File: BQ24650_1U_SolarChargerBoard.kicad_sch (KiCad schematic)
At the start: 33 parts, among them J1 Solar IO, J2 Battery IO, Q1 Q_NMOS_GDS, Q2 Q_NMOS_GDS, Q3 Q_NMOS_GDS, U1 BQ24650

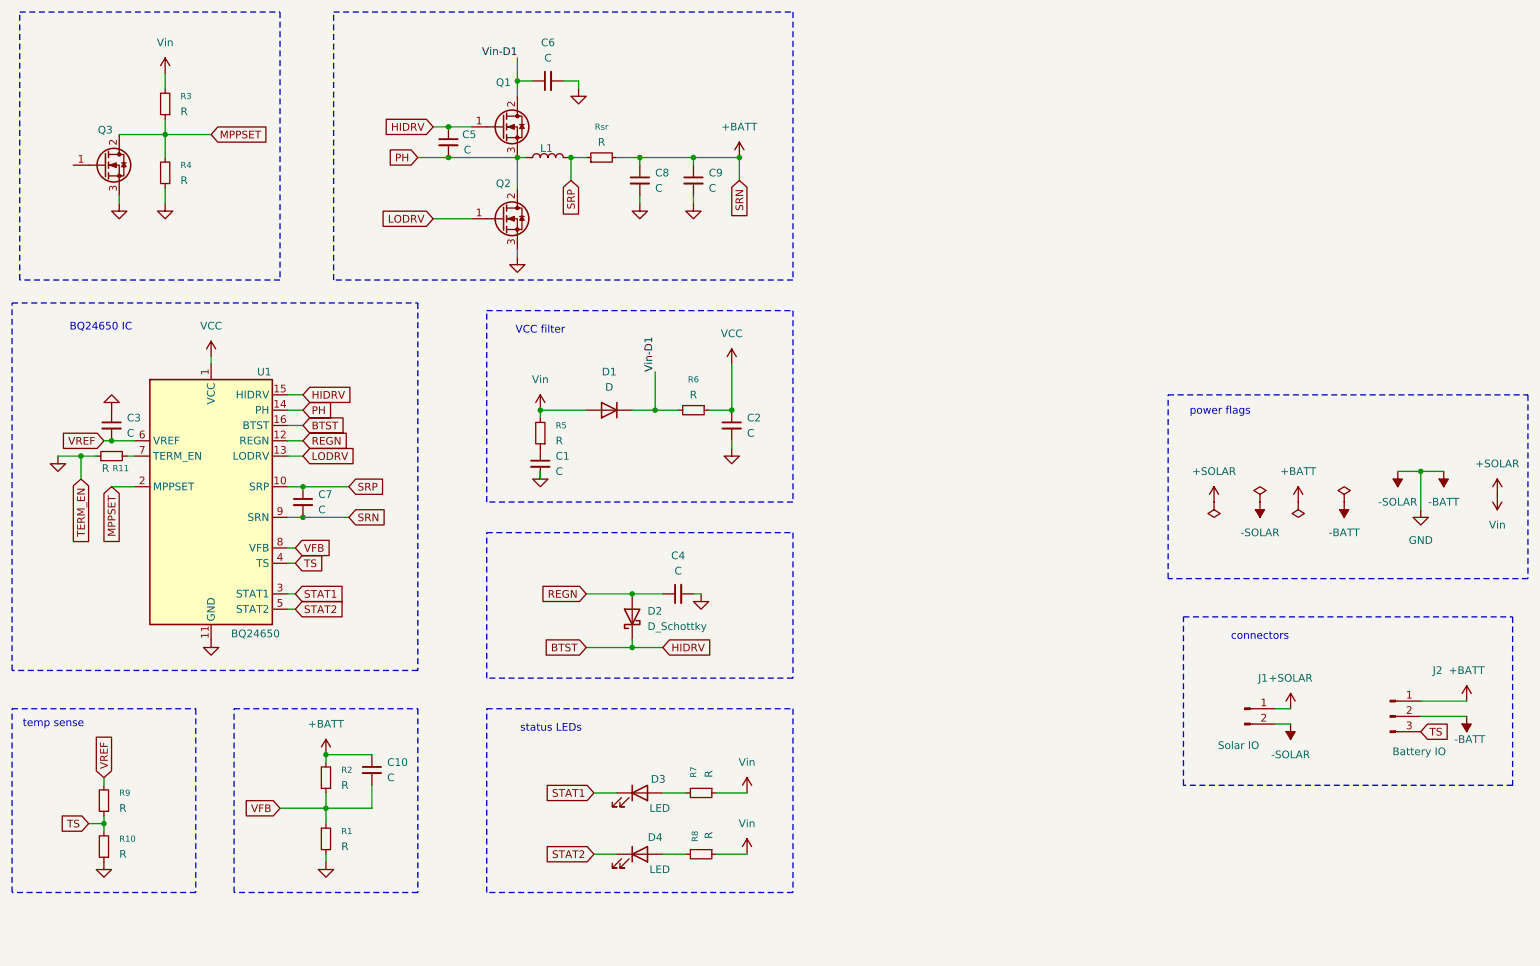
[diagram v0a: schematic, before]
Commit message: added potentiometers
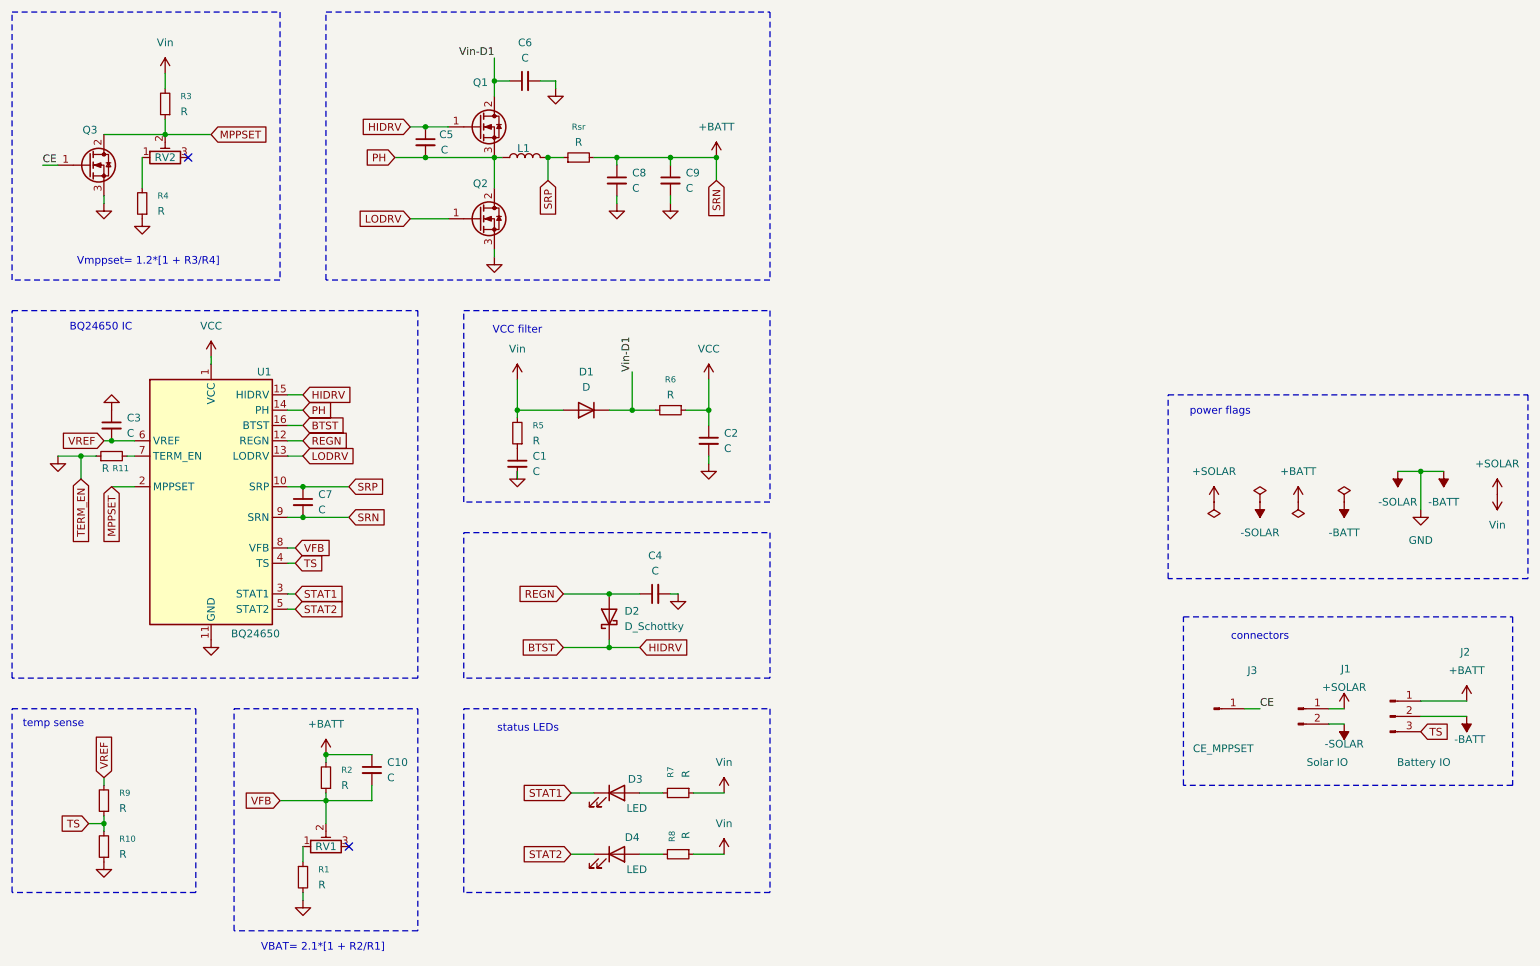
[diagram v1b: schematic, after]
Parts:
- added J3: CE_MPPSET, symbol Connector:Conn_01x01_Pin
- added RV1, RV2: R_Potentiometer_Trim, symbol Device:R_Potentiometer_Trim
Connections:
- net MPPSET: now also RV2.2; no longer R4.2
- net VFB: now also RV1.2; no longer R1.1
- net CE: now reaches Q3.1 (G)
- net CE: now also J3.1 (Pin_1)
- new net: R4.2, RV2.1
- new net: R1.1, RV1.1
- no-connect marks 0 -> 2
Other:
- note added: "VBAT= 2.1*[1 + R2/R1]"
- note added: "Vmppset= 1.2*[1 + R3/R4]"
- moved on the sheet: C1, C2, C4, C5, C6, C8, C9, D1, D2, D3, D4, J1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
